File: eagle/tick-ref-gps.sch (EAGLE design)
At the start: 48 parts, among them CN1 1PPS Out, CN2 ISP, CN3 RS232, CN4 Power In, CN5 Serial Program, U1 ATMEGA168-AU, U2 AS1115, U3 MAX232, U4 LM2931_FIXED, X1 16MHz

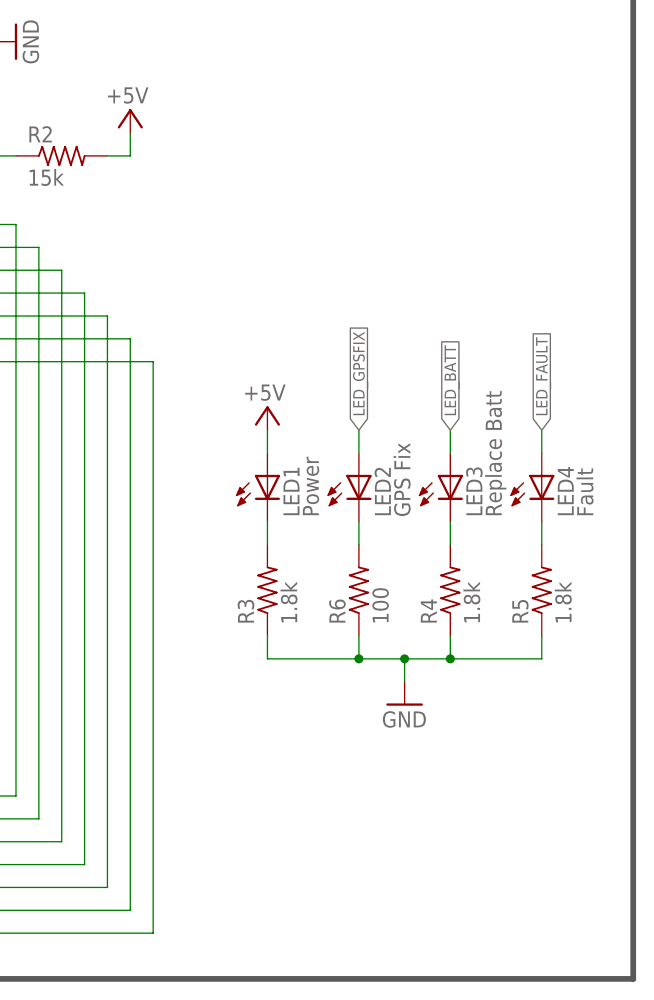
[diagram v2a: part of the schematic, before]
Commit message: Completed routing and silk, still needs final checklist run before CAMing.
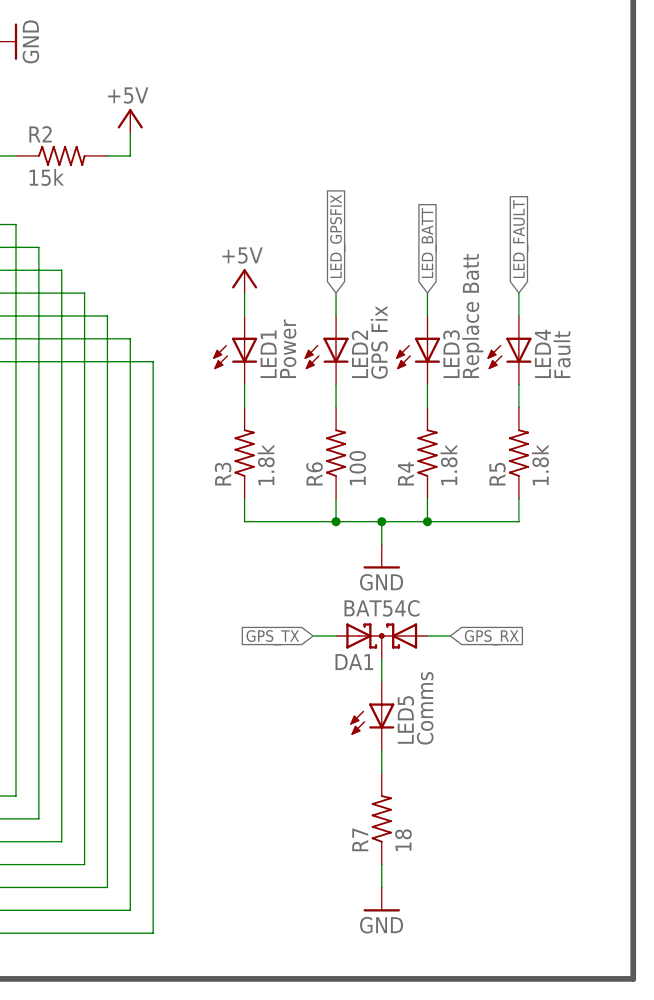
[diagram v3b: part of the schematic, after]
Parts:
- added DA1: BAT54C, diode:BAT54C
- added LED5: Comms, led:LED5MM
- added R7: 18, rcl:R-US_R0603
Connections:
- new net LED5_D: DA1.CC, LED5.A
- new net LED5_R: LED5.C, R7.2
- net GND: now also R7.1
- net GPS_RX: now also DA1.A1
- net GPS_TX: now also DA1.A2
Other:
- moved on the sheet: LED1, LED2, LED3, LED4, R3, R4, R5, R6
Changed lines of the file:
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@@
 <part name="GND17" library="supply1" deviceset="GND" device=""/>
 <part name="JP3" library="SparkFun" deviceset="JUMPER-2" device="SMD-NO" value="Standalone/PC"/>
+<part name="LED5" library="led" deviceset="LED" device="5MM" value="Comms"/>
+<part name="R7" library="rcl" deviceset="R-US_" device="R0603" value="18"/>
+<part name="GND18" library="supply1" deviceset="GND" device=""/>
+<part name="DA1" library="diode" deviceset="BAT54C" device=""/>
 </parts>
 <sheets>
@@
 <attribute name="VALUE" x="92.964" y="58.039" size="1.778" layer="96"/>
 </instance>
-<instance part="LED1" gate="G$1" x="327.66" y="55.88"/>
-<instance part="P+9" gate="1" x="327.66" y="63.5" smashed="yes">
-<attribute name="VALUE" x="329.692" y="66.04" size="1.778" layer="96" rot="R180"/>
-</instance>
-<instance part="GND12" gate="1" x="342.9" y="30.48"/>
-<instance part="LED2" gate="G$1" x="337.82" y="55.88"/>
-<instance part="LED3" gate="G$1" x="347.98" y="55.88"/>
-<instance part="LED4" gate="G$1" x="358.14" y="55.88"/>
-<instance part="R3" gate="G$1" x="327.66" y="43.18" rot="R90"/>
-<instance part="R4" gate="G$1" x="347.98" y="43.18" rot="R90"/>
-<instance part="R5" gate="G$1" x="358.14" y="43.18" rot="R90"/>
-<instance part="R6" gate="G$1" x="337.82" y="43.18" rot="R90"/>
+<instance part="LED1" gate="G$1" x="325.12" y="71.12"/>
+<instance part="P+9" gate="1" x="325.12" y="78.74" smashed="yes">
+<attribute name="VALUE" x="327.152" y="81.28" size="1.778" layer="96" rot="R180"/>
+</instance>
+<instance part="GND12" gate="1" x="340.36" y="45.72"/>
+<instance part="LED2" gate="G$1" x="335.28" y="71.12"/>
+<instance part="LED3" gate="G$1" x="345.44" y="71.12"/>
+<instance part="LED4" gate="G$1" x="355.6" y="71.12"/>
+<instance part="R3" gate="G$1" x="325.12" y="58.42" rot="R90"/>
+<instance part="R4" gate="G$1" x="345.44" y="58.42" rot="R90"/>
+<instance part="R5" gate="G$1" x="355.6" y="58.42" rot="R90"/>
+<instance part="R6" gate="G$1" x="335.28" y="58.42" rot="R90"/>
 <instance part="C9" gate="G$1" x="15.24" y="33.02"/>
 <instance part="C10" gate="G$1" x="7.62" y="33.02" rot="MR0"/>
@@
 <attribute name="VALUE" x="109.601" y="29.464" size="1.778" layer="96" rot="R90"/>
 </instance>
+<instance part="LED5" gate="G$1" x="340.36" y="30.48"/>
+<instance part="R7" gate="G$1" x="340.36" y="17.78" rot="R90"/>
+<instance part="GND18" gate="1" x="340.36" y="7.62"/>
+<instance part="DA1" gate="G$1" x="340.36" y="38.1" rot="R180"/>
 </instances>
 <busses>
@@
 <pinref part="LED1" gate="G$1" pin="A"/>
 <pinref part="P+9" gate="1" pin="+5V"/>
-<wire x1="327.66" y1="60.96" x2="327.66" y2="58.42" width="0.1524" layer="91"/>
+<wire x1="325.12" y1="76.2" x2="325.12" y2="73.66" width="0.1524" layer="91"/>
 </segment>
 <segment>
@@
 <segment>
 <pinref part="R5" gate="G$1" pin="1"/>
-<wire x1="358.14" y1="38.1" x2="358.14" y2="35.56" width="0.1524" layer="91"/>
+<wire x1="355.6" y1="53.34" x2="355.6" y2="50.8" width="0.1524" layer="91"/>
 <pinref part="R3" gate="G$1" pin="1"/>
-<wire x1="358.14" y1="35.56" x2="347.98" y2="35.56" width="0.1524" layer="91"/>
-<wire x1="347.98" y1="35.56" x2="342.9" y2="35.56" width="0.1524" layer="91"/>
-<wire x1="342.9" y1="35.56" x2="337.82" y2="35.56" width="0.1524" layer="91"/>
-<wire x1="337.82" y1="35.56" x2="327.66" y2="35.56" width="0.1524" layer="91"/>
-<wire x1="327.66" y1="35.56" x2="327.66" y2="38.1" width="0.1524" layer="91"/>
+<wire x1="355.6" y1="50.8" x2="345.44" y2="50.8" width="0.1524" layer="91"/>
+<wire x1="345.44" y1="50.8" x2="340.36" y2="50.8" width="0.1524" layer="91"/>
+<wire x1="340.36" y1="50.8" x2="335.28" y2="50.8" width="0.1524" layer="91"/>
+<wire x1="335.28" y1="50.8" x2="325.12" y2="50.8" width="0.1524" layer="91"/>
+<wire x1="325.12" y1="50.8" x2="325.12" y2="53.34" width="0.1524" layer="91"/>
 <pinref part="R4" gate="G$1" pin="1"/>
-<wire x1="347.98" y1="38.1" x2="347.98" y2="35.56" width="0.1524" layer="91"/>
-<junction x="347.98" y="35.56"/>
+<wire x1="345.44" y1="53.34" x2="345.44" y2="50.8" width="0.1524" layer="91"/>
+<junction x="345.44" y="50.8"/>
 <pinref part="GND12" gate="1" pin="GND"/>
-<wire x1="342.9" y1="33.02" x2="342.9" y2="35.56" width="0.1524" layer="91"/>
-<junction x="342.9" y="35.56"/>
+<wire x1="340.36" y1="48.26" x2="340.36" y2="50.8" width="0.1524" layer="91"/>
+<junction x="340.36" y="50.8"/>
 <pinref part="R6" gate="G$1" pin="1"/>
-<wire x1="337.82" y1="38.1" x2="337.82" y2="35.56" width="0.1524" layer="91"/>
-<junction x="337.82" y="35.56"/>
+<wire x1="335.28" y1="53.34" x2="335.28" y2="50.8" width="0.1524" layer="91"/>
+<junction x="335.28" y="50.8"/>
 </segment>
 <segment>
@@
 <junction x="17.78" y="127"/>
 </segment>
+<segment>
+<pinref part="R7" gate="G$1" pin="1"/>
+<pinref part="GND18" gate="1" pin="GND"/>
+<wire x1="340.36" y1="10.16" x2="340.36" y2="12.7" width="0.1524" layer="91"/>
+</segment>
 </net>
 <net name="1PPS" class="0">
@@
 <segment>
 <pinref part="LED2" gate="G$1" pin="A"/>
-<wire x1="337.82" y1="58.42" x2="337.82" y2="60.96" width="0.1524" layer="91"/>
-<label x="337.82" y="60.96" size="1.27" layer="95" rot="R90" xref="yes"/>
+<wire x1="335.28" y1="73.66" x2="335.28" y2="76.2" width="0.1524" layer="91"/>
+<label x="335.28" y="76.2" size="1.27" layer="95" rot="R90" xref="yes"/>
 </segment>
 </net>
@@
 <segment>
 <pinref part="LED3" gate="G$1" pin="A"/>
-<wire x1="347.98" y1="58.42" x2="347.98" y2="60.96" width="0.1524" layer="91"/>
-<label x="347.98" y="60.96" size="1.27" layer="95" rot="R90" xref="yes"/>
+<wire x1="345.44" y1="73.66" x2="345.44" y2="76.2" width="0.1524" layer="91"/>
+<label x="345.44" y="76.2" size="1.27" layer="95" rot="R90" xref="yes"/>
 </segment>
 <segment>
@@
 <label x="254" y="137.16" size="1.27" layer="95" rot="R90" xref="yes"/>
 </segment>
+<segment>
+<pinref part="DA1" gate="G$1" pin="A2"/>
+<wire x1="335.28" y1="38.1" x2="332.74" y2="38.1" width="0.1524" layer="91"/>
+<label x="332.74" y="38.1" size="1.27" layer="95" rot="R180" xref="yes"/>
+</segment>
 </net>
 <net name="GPS_RX" class="0">
@@
 <wire x1="99.06" y1="43.18" x2="99.06" y2="40.64" width="0.1524" layer="91"/>
 <label x="99.06" y="40.64" size="1.27" layer="95" rot="R270" xref="yes"/>
+</segment>
+<segment>
+<pinref part="DA1" gate="G$1" pin="A1"/>
+<wire x1="345.44" y1="38.1" x2="347.98" y2="38.1" width="0.1524" layer="91"/>
+<label x="347.98" y="38.1" size="1.27" layer="95" xref="yes"/>
 </segment>
 </net>
@@
 <segment>
 <pinref part="LED4" gate="G$1" pin="A"/>
-<wire x1="358.14" y1="58.42" x2="358.14" y2="60.96" width="0.1524" layer="91"/>
-<label x="358.14" y="60.96" size="1.27" layer="95" rot="R90" xref="yes"/>
+<wire x1="355.6" y1="73.66" x2="355.6" y2="76.2" width="0.1524" layer="91"/>
+<label x="355.6" y="76.2" size="1.27" layer="95" rot="R90" xref="yes"/>
 </segment>
 <segment>
@@
 <pinref part="R5" gate="G$1" pin="2"/>
 <pinref part="LED4" gate="G$1" pin="C"/>
-<wire x1="358.14" y1="48.26" x2="358.14" y2="50.8" width="0.1524" layer="91"/>
+<wire x1="355.6" y1="63.5" x2="355.6" y2="66.04" width="0.1524" layer="91"/>
 </segment>
 </net>
@@
 <pinref part="LED3" gate="G$1" pin="C"/>
 <pinref part="R4" gate="G$1" pin="2"/>
-<wire x1="347.98" y1="50.8" x2="347.98" y2="48.26" width="0.1524" layer="91"/>
+<wire x1="345.44" y1="66.04" x2="345.44" y2="63.5" width="0.1524" layer="91"/>
 </segment>
 </net>
@@
 <pinref part="R3" gate="G$1" pin="2"/>
 <pinref part="LED1" gate="G$1" pin="C"/>
-<wire x1="327.66" y1="48.26" x2="327.66" y2="50.8" width="0.1524" layer="91"/>
+<wire x1="325.12" y1="63.5" x2="325.12" y2="66.04" width="0.1524" layer="91"/>
 </segment>
 </net>
@@
 <pinref part="LED2" gate="G$1" pin="C"/>
 <pinref part="R6" gate="G$1" pin="2"/>
-<wire x1="337.82" y1="50.8" x2="337.82" y2="48.26" width="0.1524" layer="91"/>
-</segment>
-</net>
+<wire x1="335.28" y1="66.04" x2="335.28" y2="63.5" width="0.1524" layer="91"/>
+</segment>
+</net>
+<net name="LED5_R" class="0">
+<segment>
+<pinref part="LED5" gate="G$1" pin="C"/>
+<pinref part="R7" gate="G$1" pin="2"/>
+<wire x1="340.36" y1="25.4" x2="340.36" y2="22.86" width="0.1524" layer="91"/>
+</segment>
+</net>
+<net name="LED5_D" class="0">
+<segment>
+<pinref part="LED5" gate="G$1" pin="A"/>
+<pinref part="DA1" gate="G$1" pin="CC"/>
+<wire x1="340.36" y1="35.56" x2="340.36" y2="33.02" width="0.1524" layer="91"/>
+</segment>
+</net>
